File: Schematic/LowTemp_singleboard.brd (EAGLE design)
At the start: 100 x 86.3 mm, 31 parts, among them IC1 7805L, J1 SCREEN, SW2 EC11B-V

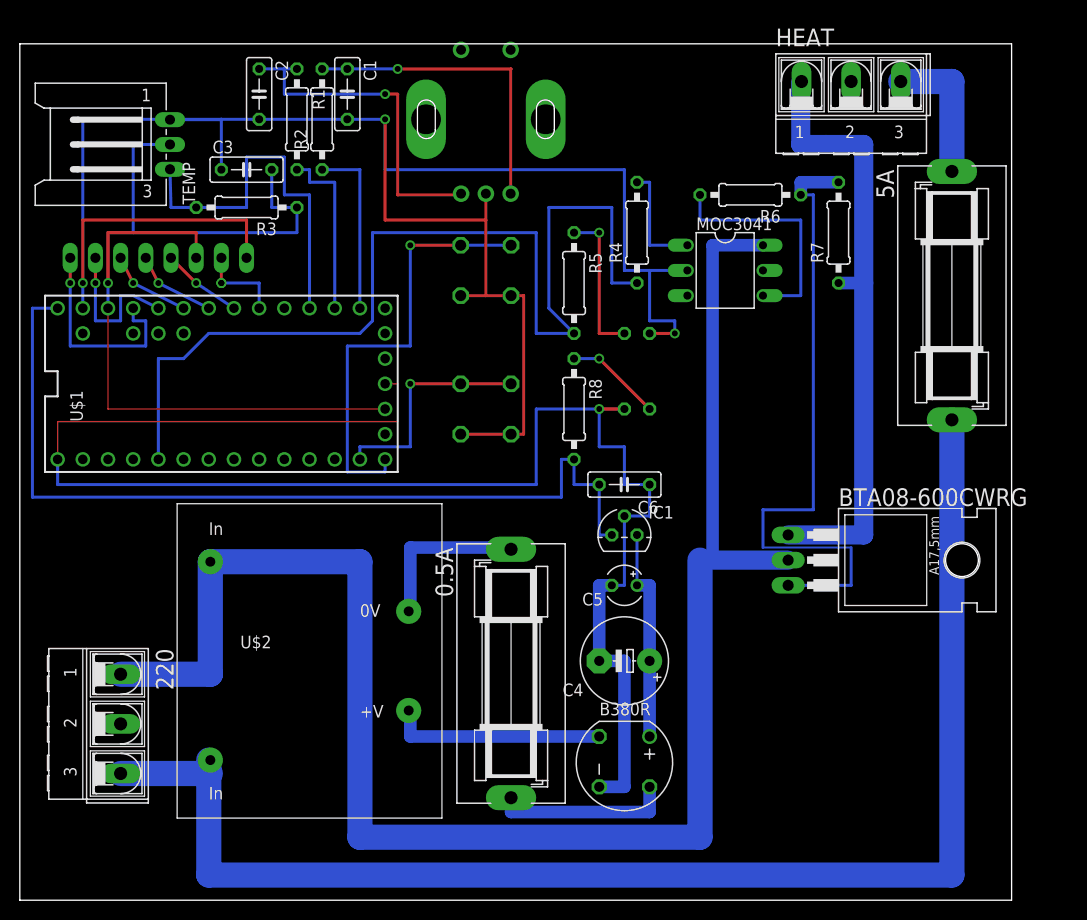
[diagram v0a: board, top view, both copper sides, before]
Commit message: Add 2 board schematic. One board for the controls (screen / button) One board for electronics part
Each board areBoards are connected together with 2x10 pin connector
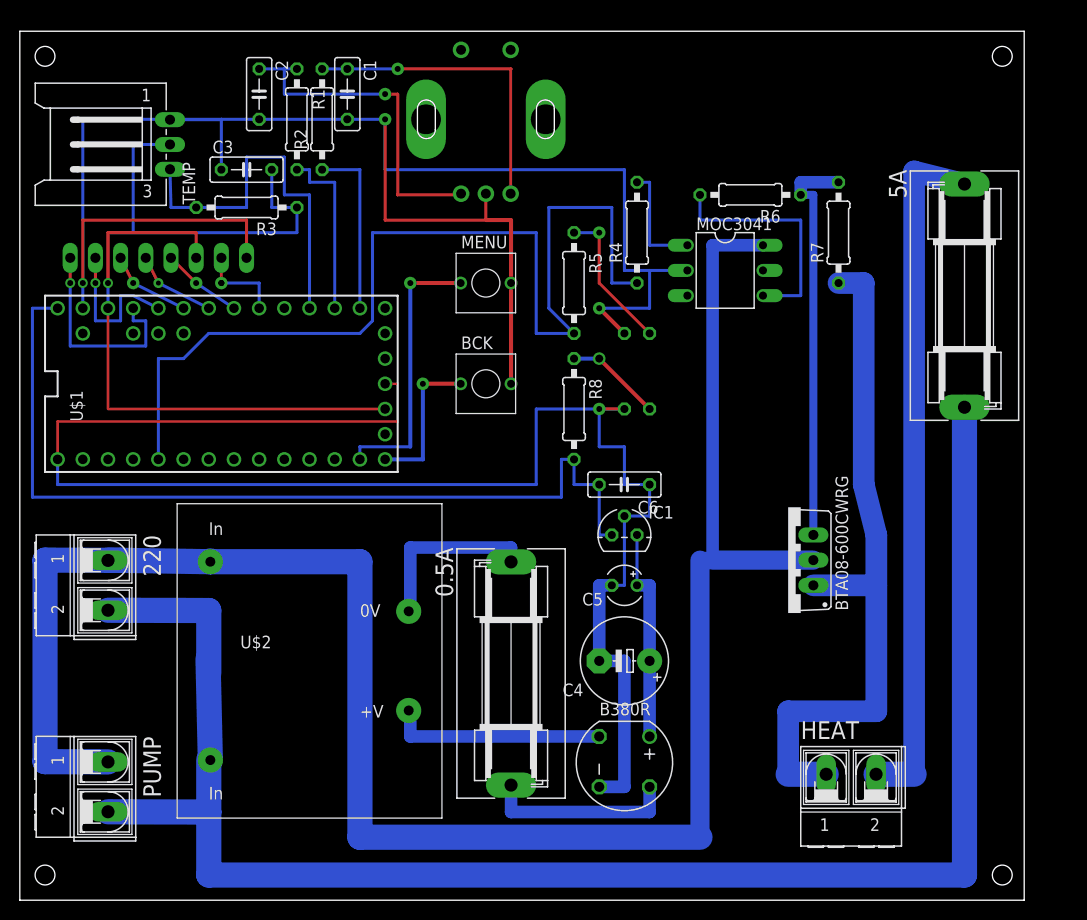
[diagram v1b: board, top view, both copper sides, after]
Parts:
- removed S1, S2: DTE6K, switch-misc:DTE6K
- added BCK, MENU: 2PIN, switch-misc:2PIN
- added PUMP: (no value), con-ptr500:AK500/2-H
- 0.5A, 5A: value FUSESH35 -> (none); device fuse:SH25 -> fuse:SH22,5A
- 220, HEAT: device con-ptr500:AK500/3-H -> con-ptr500:AK500/2-H
- BTA08-600CWRG: value BT136 -> BT138-V; device triac:TO220AB -> triac:TO220BV
- moved HEAT 69.9 mm to (83.8, 6.35)
- moved 220 14.0 mm to (8.89, 25.4)
- moved BTA08-600CWRG 6.35 mm to (77.5, 27.9), turned to 90 degrees
- moved 5A 1.27 mm to (95.2, 54.6)
- turned LRED to 0 degrees
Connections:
- new net 220AC: 220.1
- net 220VA: now also BTA08-600CWRG.T2, PUMP.1; no longer 220.1, BTA08-600CWRG.2
- net 220VC: now also 220.2, PUMP.2; no longer 220.3
- net AGND: now also BCK.2, MENU.2; no longer S1.1, S1.2, S2.1, S2.2
- net BTBCK: now also BCK.1; no longer S2.3, S2.4
- net BTMENU: now also MENU.1; no longer S1.3, S1.4
- net N$6: now also BTA08-600CWRG.G; no longer BTA08-600CWRG.3
- net N$8: now also BTA08-600CWRG.T1; no longer BTA08-600CWRG.1
- net N$9: now also HEAT.2; no longer HEAT.3
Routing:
- net N$9: track 14.2 -> 69.9 mm
- net BTBCK: track 44.4 -> 15.2 mm
- net 220VC: track 143.0 -> 172.0 mm
- net 220VA: track 171.2 -> 198.0 mm
- net N$6: track 66.0 -> 40.6 mm
- net AGND: track 200.9 -> 186.7 mm
- net N$8: track 62.3 -> 71.3 mm
- net BTMENU: track 22.9 -> 27.9 mm
- net N$7: track 16.9 -> 18.2 mm
- net N$11: track 18.0 -> 19.2 mm
- net N$15: vias 0 -> 1
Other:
- board size 100 x 86.3 mm -> 101.3 x 87.6 mm
